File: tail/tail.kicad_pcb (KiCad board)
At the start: 4 copper layers, 102.8 x 200 mm, 5 parts

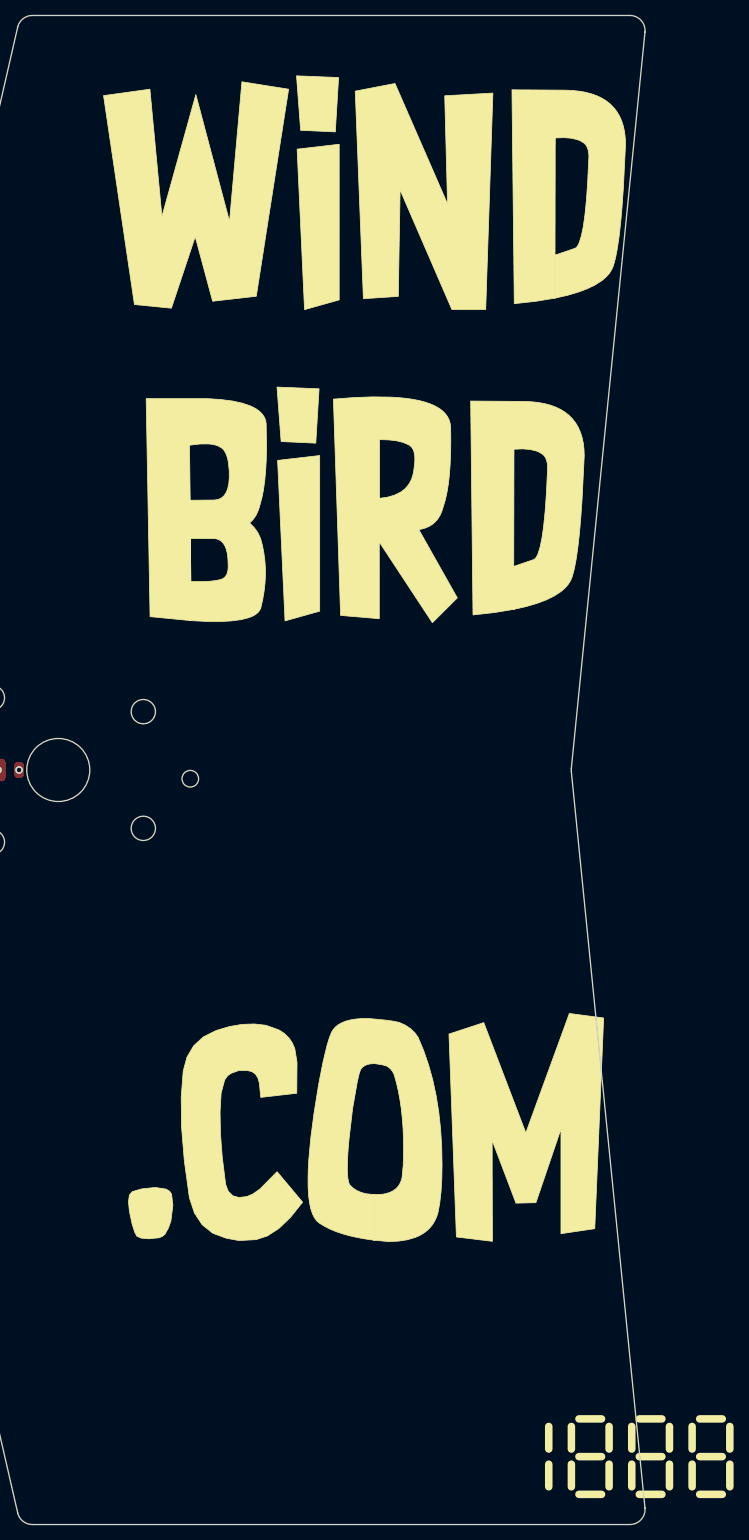
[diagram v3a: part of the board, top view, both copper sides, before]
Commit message: New artwork, with the help of designers from nodesign.net
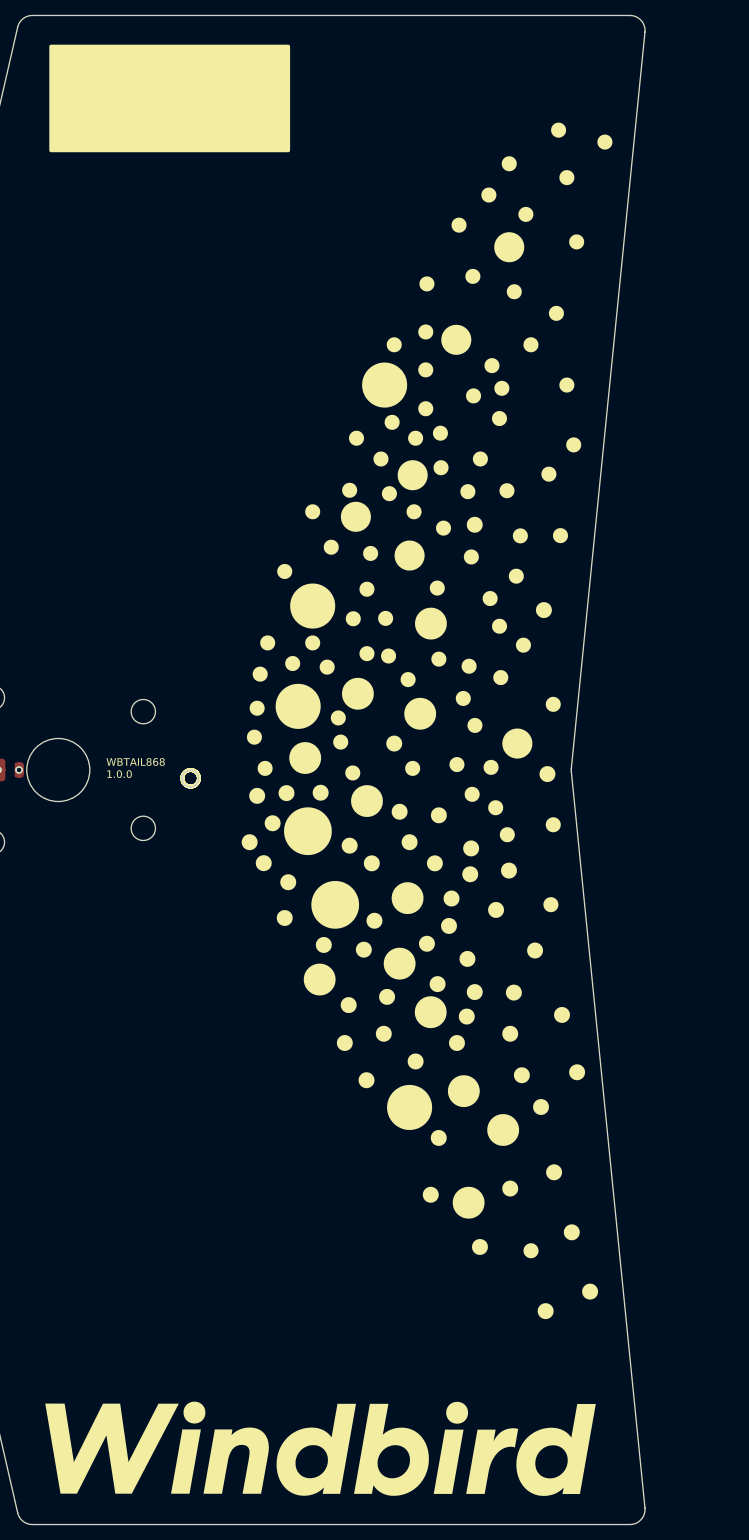
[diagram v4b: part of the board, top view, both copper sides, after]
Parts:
- removed the REF** at (74.0, 43.0)
- removed the REF** at (144.0, 42.5)
- removed the REF** at (69.0, 228.0)
- removed the REF** at (78.0, 228.0)
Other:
- board text added: "WBTAIL868 1.0.0"
